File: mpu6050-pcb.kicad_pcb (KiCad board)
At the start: 2 copper layers, 9 parts, among them U1 MPU-6050

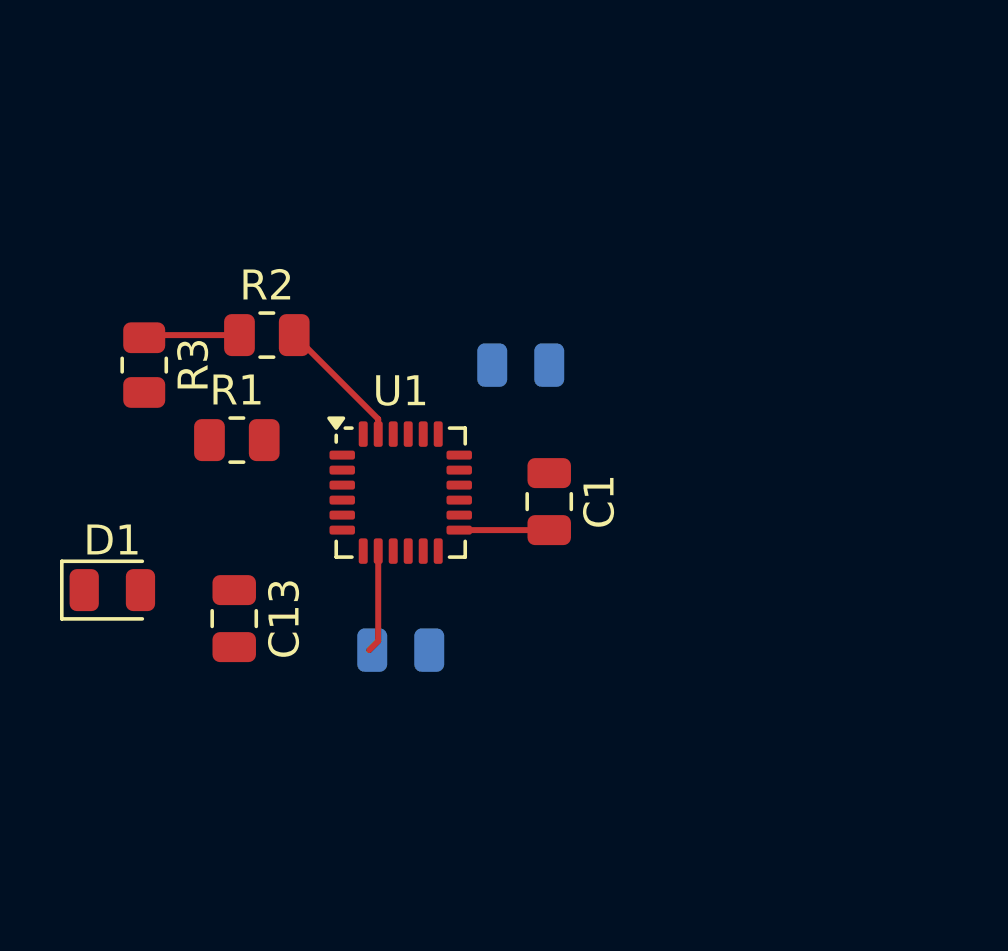
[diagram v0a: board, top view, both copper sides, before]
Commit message: updated schematic and changed routing
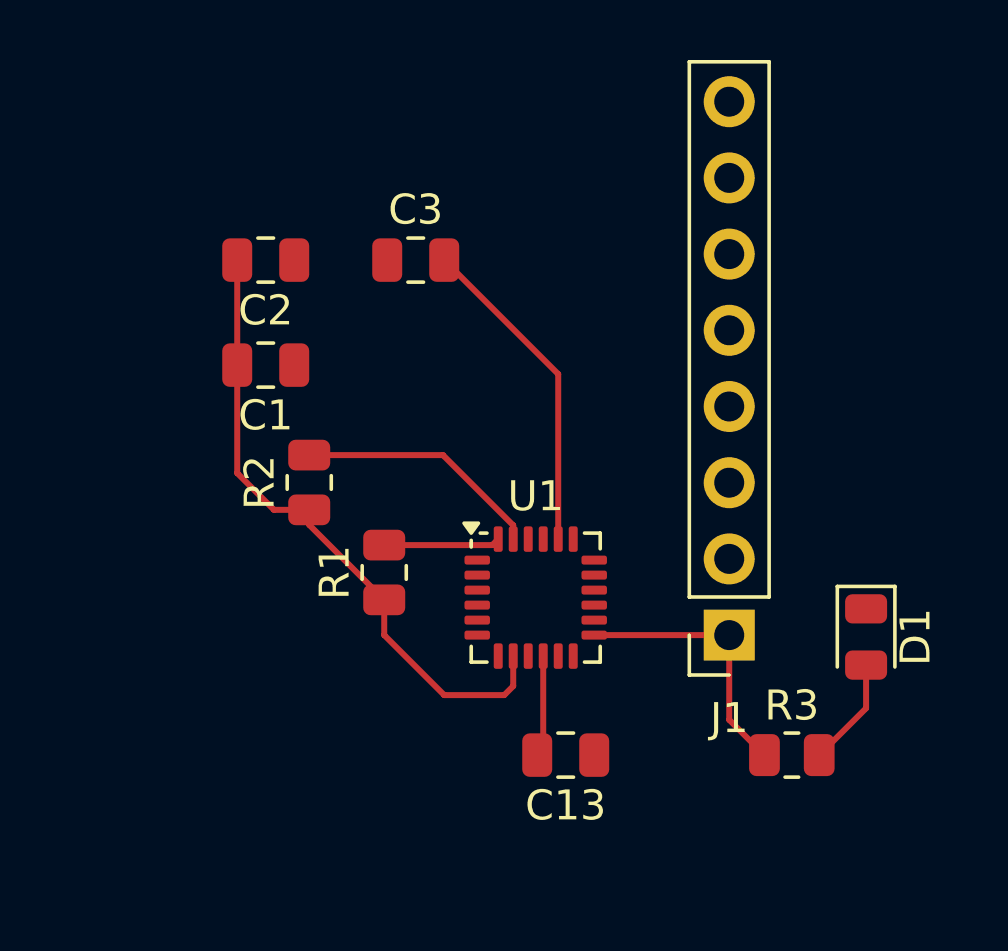
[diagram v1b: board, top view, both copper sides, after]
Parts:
- added J1: Conn_01x08_Socket, Connector_PinSocket_2.54mm:PinSocket_1x08_P2.54mm_Vertical, F.Cu at (160.5, 106.0)
- C2, C3: moved to F.Cu
- moved R3 25.2 mm to (162.6, 110.0), turned to 0 degrees
- moved D1 25.2 mm to (165.1, 106.1), turned to -90 degrees
- moved C2 13.8 mm to (145.1, 93.5)
- moved C13 12.0 mm to (155.1, 110.0), turned to 180 degrees
- moved C1 10.5 mm to (145.1, 97.0), turned to 180 degrees
- moved R1 6.60 mm to (149.0, 103.9), turned to 90 degrees
- moved U1 5.70 mm to (154.1, 104.8)
- moved R2 5.11 mm to (146.5, 100.9), turned to 90 degrees
- moved C3 4.95 mm to (150.1, 93.5), turned to 0 degrees
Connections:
- U1 pad 12: unconnected-(U1-INT-Pad12) -> Net-(J1-Pin_8)
- U1 pad 6: unconnected-(U1-AUX_DA-Pad6) -> Net-(J1-Pin_5)
- U1 pad 7: unconnected-(U1-AUX_CL-Pad7) -> Net-(J1-Pin_6)
- U1 pad 9: unconnected-(U1-AD0-Pad9) -> Net-(J1-Pin_7)
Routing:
- net 3V3: track 9.64 -> 30.5 mm
- net Net-(U1-CPOUT): track 0.00 -> 10.9 mm
- net Net-(J1-Pin_4): track 0.00 -> 3.88 mm
- net Net-(J1-Pin_3): track 4.46 -> 8.23 mm
- net Net-(D1-A): track 0.00 -> 3.65 mm
- net Net-(U1-REGOUT): track 0.00 -> 3.38 mm

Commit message: changed routing and connector type
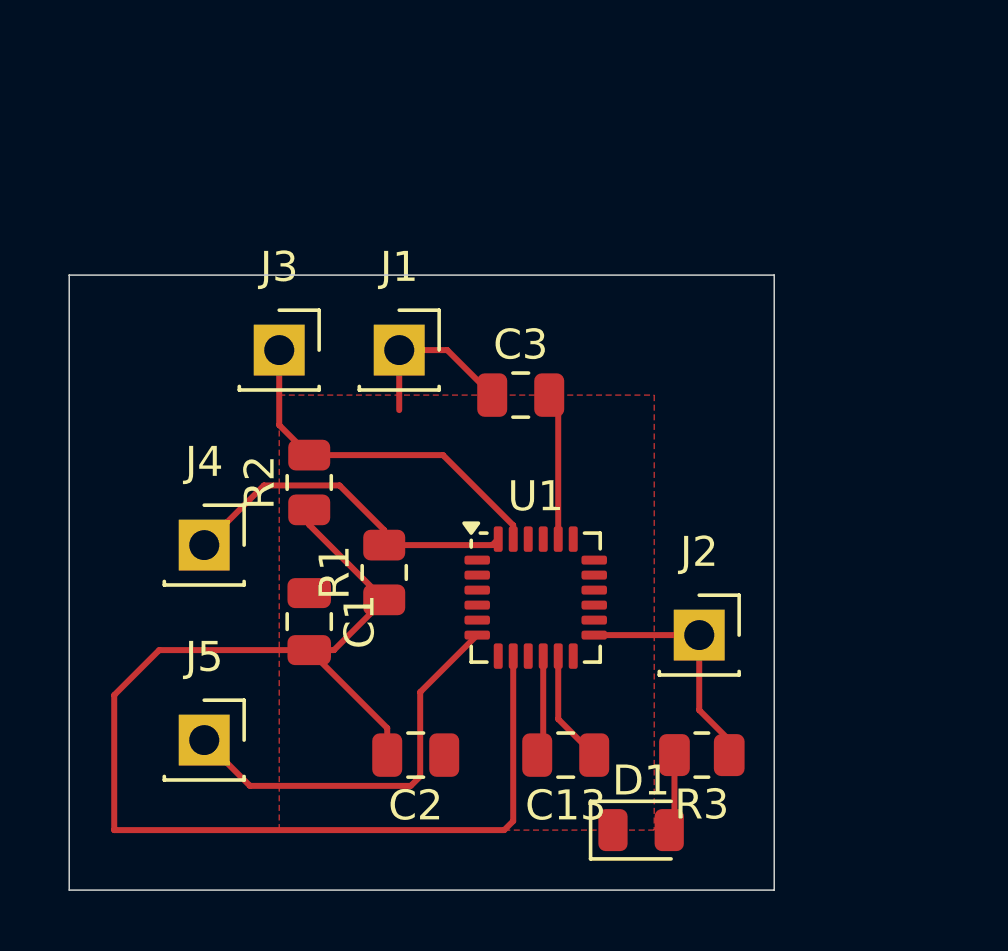
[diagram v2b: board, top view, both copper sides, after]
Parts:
- added J2: Conn_01x01_Socket, Connector_PinSocket_2.54mm:PinSocket_1x01_P2.54mm_Vertical, F.Cu at (159.5, 106.0)
- added J3: Conn_01x01_Socket, Connector_PinSocket_2.54mm:PinSocket_1x01_P2.54mm_Vertical, F.Cu at (145.5, 96.5)
- added J4: Conn_01x01_Socket, Connector_PinSocket_2.54mm:PinSocket_1x01_P2.54mm_Vertical, F.Cu at (143.0, 103.0)
- added J5: Conn_01x01_Socket, Connector_PinSocket_2.54mm:PinSocket_1x01_P2.54mm_Vertical, F.Cu at (143.0, 109.5)
- J1: value Conn_01x08_Socket -> Conn_01x01_Socket; footprint Connector_PinSocket_2.54mm:PinSocket_1x08_P2.54mm_Vertical -> Connector_PinSocket_2.54mm:PinSocket_1x01_P2.54mm_Vertical
- moved C2 17.2 mm to (150.1, 110.0)
- moved J1 14.5 mm to (149.5, 96.5), turned to 0 degrees
- moved D1 9.88 mm to (157.6, 112.5), turned to 0 degrees
- moved C1 8.67 mm to (146.5, 105.5), turned to -90 degrees
- moved C3 5.70 mm to (153.6, 98.0)
- moved R3 3.00 mm to (159.6, 110.0), turned to 180 degrees
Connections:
- J1 pad 1: 3V3 -> GND
- R1 pad 2: Net-(J1-Pin_4) -> Net-(J4-Pin_1)
- R2 pad 2: Net-(J1-Pin_3) -> Net-(J3-Pin_1)
- U1 pad 12: Net-(J1-Pin_8) -> Net-(J8-Pin_1)
- U1 pad 23: Net-(J1-Pin_3) -> Net-(J3-Pin_1)
- U1 pad 24: Net-(J1-Pin_4) -> Net-(J4-Pin_1)
- U1 pad 6: Net-(J1-Pin_5) -> Net-(J5-Pin_1)
- U1 pad 7: Net-(J1-Pin_6) -> Net-(J6-Pin_1)
- U1 pad 9: Net-(J1-Pin_7) -> Net-(J7-Pin_1)
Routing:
- net 3V3: track 30.5 -> 50.3 mm
- net Net-(J5-Pin_1): track 0.00 -> 13.5 mm
- net Net-(J3-Pin_1): track 0.00 -> 12.1 mm
- net Net-(J4-Pin_1): track 0.00 -> 11.8 mm
- net GND: track 0.00 -> 9.57 mm
- net Net-(J1-Pin_3): track 8.23 -> 0.00 mm
- net Net-(U1-CPOUT): track 10.9 -> 4.92 mm
- net Net-(J1-Pin_4): track 3.88 -> 0.00 mm
- net Net-(D1-A): track 3.65 -> 2.57 mm
- added copper zone on F.Cu, net GND
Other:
- board outline added: 23.5 x 20.5 mm
